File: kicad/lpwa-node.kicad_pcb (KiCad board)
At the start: 4 copper layers, 85 x 55 mm, 72 parts, among them J1 USB_C_ESP, J2 I2C, J3 USB to VBAT, J4 USB_C_SIM, J5 SIM_Card, J6 MEAS, J8 LTE, SW1 BOOT, SW2 USER, U1 TPS7A0230PDBVR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

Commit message: Draft
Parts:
- removed J2: I2C, Connector_PinHeader_2.54mm:PinHeader_2x02_P2.54mm_Vertical_SMD
- removed J3: USB to VBAT, Connector_PinHeader_2.54mm:PinHeader_1x03_P2.54mm_Vertical
- added C20: 10µF, Capacitor_SMD:C_0603_1608Metric, F.Cu at (65.0, 92.0)
- added C21: 10µF, Capacitor_SMD:C_0603_1608Metric, F.Cu at (65.8, 94.6)
- added JP11: VSYS_BYPASS, Jumper:SolderJumper-2_P1.3mm_Open_RoundedPad1.0x1.5mm, F.Cu at (53.7, 93.6)
- added R18: 100k, Resistor_SMD:R_0603_1608Metric, F.Cu at (61.5, 92.0)
- added R19: 732k, Resistor_SMD:R_0603_1608Metric, F.Cu at (61.5, 90.2)
- added R20: 1M, Resistor_SMD:R_0603_1608Metric, F.Cu at (57.5, 94.5)
- added R21: 10k, Resistor_SMD:R_0603_1608Metric, F.Cu at (57.5, 96.5)
- added TP10: SDA, TestPoint:TestPoint_Pad_D1.5mm, F.Cu at (76.5, 95.1)
- added TP11: USB_5V, TestPoint:TestPoint_Pad_D1.5mm, F.Cu at (60.5, 95.8)
- added TP12: VSYS, TestPoint:TestPoint_Pad_D1.5mm, F.Cu at (53.2, 88.0)
- added TP7: 3V0, TestPoint:TestPoint_Pad_D1.5mm, F.Cu at (53.2, 83.3)
- added TP8: GND, TestPoint:TestPoint_Pad_D1.5mm, F.Cu at (53.2, 71.0)
- added TP9: SCL, TestPoint:TestPoint_Pad_D1.5mm, F.Cu at (76.5, 93.2)
- added U10: LM66100DCK, Package_TO_SOT_SMD:SOT-363_SC-70-6, F.Cu at (57.5, 99.0)
- added U11: LM66100DCK, Package_TO_SOT_SMD:SOT-363_SC-70-6, F.Cu at (57.5, 92.0)
- added U9: TLV75901PDRVR, lpwa-node:WSON-6_L2.0-W2.0-P0.65-TL-EP, F.Cu at (63.2, 94.5)
- JP10: value SIM USB VBUS -> SIM_USB_VBUS
- moved C7 12.7 mm to (63.8, 87.0)
- moved R8 12.7 mm to (59.8, 87.0)
- moved R9 12.7 mm to (61.8, 87.0)
- moved C4 11.0 mm to (73.0, 94.5)
- moved U2 5.00 mm to (70.1, 93.6)
- moved D3 4.56 mm to (54.8, 99.0), turned to -90 degrees
- moved SW1 4.00 mm to (70.0, 87.5)
- moved C1 3.04 mm to (56.0, 89.0)
- moved U1 2.80 mm to (56.0, 85.8)
- moved C3 2.55 mm to (56.0, 82.5)
- moved TP6 1.88 mm to (76.3, 87.2)
- moved TP3 0.93 mm to (81.5, 73.4)
- moved TP5 0.70 mm to (78.3, 85.5)
- moved C2 0.50 mm to (56.0, 78.5)
- moved R2 0.50 mm to (56.0, 80.5)
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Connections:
- net +3V3 renamed 3V0
- C1 pad 2: +BATT -> VSYS
- C10 pad 2: +BATT -> VSYS
- C11 pad 2: +BATT -> VSYS
- C13 pad 2: +BATT -> VSYS
- C8 pad 2: +BATT -> VSYS
- D3 pad 1: +BATT -> BATTERY
- R8 pad 1: +BATT -> BATTERY
- U1 pad 1: +BATT -> VSYS
- U1 pad 3: +BATT -> VSYS
- U5 pad 4: +BATT -> BATTERY
- U6 pad 34: +BATT -> VSYS
- U6 pad 35: +BATT -> VSYS
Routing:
- net VSYS: track 0.00 -> 106.0 mm, vias 0 -> 6
- net +BATT: track 97.4 -> 0.00 mm, vias 5 -> 0
- net 3V0: track 160.2 -> 126.7 mm, vias 3 -> 4
- net BATTERY: track 0.00 -> 32.3 mm, vias 0 -> 3
- net /SIM7080/SIM_USB_VBUS: track 15.8 -> 30.6 mm
- net USB_ESP_+5V: track 34.9 -> 20.8 mm
- net ESP_VBAT_ADC: track 41.7 -> 30.5 mm
- net USB_4V6: track 0.00 -> 11.1 mm
- net Net-(U10-~{CE}): track 0.00 -> 10.9 mm
- net /BOOT: track 40.0 -> 45.2 mm
- net ESP_USB_D+: track 27.7 -> 22.7 mm
- net ESP_USB_D-: track 27.7 -> 22.9 mm
- net Net-(U9-FB): track 0.00 -> 4.29 mm
- net /D+: track 7.03 -> 11.3 mm
- net /D-: track 5.84 -> 8.87 mm
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- added copper zone on F.Cu, net USB_ESP_+5V
- added copper zone on F.Cu, net VSYS
- removed copper zone on F.Cu, net +BATT
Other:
- outline, holes or cut-outs redrawn
- board text added: "NiMH Rechargeable = Best Alkaline = OK Lithium 1.5V = NOT ALLOWED!"

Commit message: Draft
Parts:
- removed TP3: ESP_SIM_RI, TestPoint:TestPoint_Pad_D1.5mm
- added C22: 100µF, Capacitor_SMD:C_1206_3216Metric, F.Cu at (100.5, 46.5)
- added R23: 1M, Resistor_SMD:R_0603_1608Metric, F.Cu at (79.0, 79.5)
- added R24: 732k, Resistor_SMD:R_0603_1608Metric, F.Cu at (77.0, 79.5)
- added TP13: PWRKEY, TestPoint:TestPoint_Pad_D1.5mm, F.Cu at (93.8, 50.4)
- added TP14: STATUS, TestPoint:TestPoint_Pad_D1.5mm, F.Cu at (97.8, 52.2)
- added TP15: NETLIGHT, TestPoint:TestPoint_Pad_D1.5mm, F.Cu at (92.1, 48.5)
- moved D2 24.3 mm to (87.7, 59.8), turned to 0 degrees
- moved D4 20.4 mm to (96.0, 49.6)
- moved R1 20.2 mm to (83.0, 59.8)
- moved U4 20.0 mm to (129.0, 80.0)
- moved C6 20.0 mm to (126.0, 80.0)
- moved C1 20.0 mm to (56.0, 69.0)
- moved C10 20.0 mm to (110.0, 47.0)
- moved C11 20.0 mm to (106.5, 46.5)
- moved C12 20.0 mm to (89.2, 51.5)
- moved C13 20.0 mm to (103.5, 46.5)
- moved C14 20.0 mm to (82.5, 78.6)
- moved C15 20.0 mm to (102.0, 74.5)
- moved C17 20.0 mm to (123.0, 55.0)
- moved C19 20.0 mm to (125.5, 52.5)
- moved C2 20.0 mm to (56.0, 58.5)
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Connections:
- U3 pad 18: ESP_SIM_RI -> ESP_USB_SENSE
- U6 pad 41: unconnected-(U6-NETLIGHT-Pad41) -> Net-(U6-NETLIGHT)
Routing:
- net ESP_USB_SENSE: track 0.00 -> 40.3 mm, vias 0 -> 2
- net VSYS: track 106.0 -> 83.1 mm, vias 6 -> 7
- net Net-(U6-NETLIGHT): track 0.00 -> 15.5 mm, vias 0 -> 2
- net USB_ESP_+5V: track 20.8 -> 33.2 mm
- net 3V0: track 126.7 -> 117.8 mm
- net GND: track 21.2 -> 16.1 mm, vias 90 -> 105
- net SCL: track 94.1 -> 89.7 mm
- net ESP_SIM_RI: track 4.07 -> 0.00 mm
- net SIM_STATUS: track 7.88 -> 11.0 mm
- net Net-(U5-Pad2): track 77.8 -> 79.2 mm
- net ESP_BTN: track 22.5 -> 23.5 mm
- net SIM_PWRKEY: track 44.6 -> 45.4 mm
- net SDA: track 80.3 -> 81.0 mm
- added copper zone on F.Cu, net 3V0
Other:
- board size 85 x 55 mm -> 84 x 50 mm
- board text added: "ENGINEERING SAMPLE NOT FOR RESALE NOT CERTIFIED"
- board text added: "https://github.com/MikkoTervala/ lpwa-node-hardware"
- board text added: "⌀ 2.6mm"
- board text removed: "NiMH Rechargeable = Best Alkaline = OK Lithium 1.5V = NOT ALLOWED!"

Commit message: First orderable version
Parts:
- added D7: ESD5Z3.3T1G, Diode_SMD:D_SOD-523, F.Cu at (115.5, 80.0)
- added D8: ESD5Z3.3T1G, Diode_SMD:D_SOD-523, F.Cu at (112.0, 80.0)
- added D9: ESD5Z3.3T1G, Diode_SMD:D_SOD-523, F.Cu at (113.8, 80.0)
- added R22: 10k, Resistor_SMD:R_0603_1608Metric, F.Cu at (89.2, 49.5)
- added R25: 100k, Resistor_SMD:R_0603_1608Metric, F.Cu at (90.0, 59.2)
- C6: value 100nF -> 10µF
- moved R14 4.60 mm to (112.8, 74.8), turned to 180 degrees
- moved R13 2.26 mm to (112.8, 76.8), turned to 0 degrees
- moved R6 1.53 mm to (93.9, 58.4)
- moved R7 1.53 mm to (93.9, 56.9)
- moved TP1 1.22 mm to (96.7, 57.0)
- moved TP2 1.22 mm to (96.7, 54.5)
- moved TP4 1.22 mm to (96.7, 59.5)
- moved D2 1.08 mm to (86.8, 59.2)
- moved JP10 1.00 mm to (109.0, 73.1)
- moved R11 1.00 mm to (97.6, 70.3)
- moved R1 0.60 mm to (83.0, 59.2)
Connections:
- D4 pad 1: SIM_PWRKEY -> Net-(D4-K)
- TP13 pad 1: SIM_PWRKEY -> Net-(D4-K)
- U6 pad 39: SIM_PWRKEY -> Net-(D4-K)
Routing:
- net SIM_PWRKEY: track 45.4 -> 26.5 mm
- net Net-(D4-K): track 0.00 -> 18.0 mm
- net 3V0: track 117.8 -> 125.1 mm
- net ESP_BTN: track 23.5 -> 27.0 mm
- net SDA: track 81.0 -> 83.5 mm, vias 2 -> 4
- net Net-(J4-CC2): track 9.77 -> 7.25 mm
- net /BOOT: track 45.2 -> 46.8 mm
- net SCL: track 89.7 -> 91.1 mm, vias 3 -> 5
- net Net-(J4-CC1): track 11.6 -> 10.3 mm
- net Net-(D1-A): track 7.21 -> 8.25 mm
- net USB_SIM_+5V: track 13.6 -> 14.1 mm
- net /SIM7080/SIM_USB_VBUS: track 30.6 -> 30.1 mm
- net GND: vias 105 -> 108

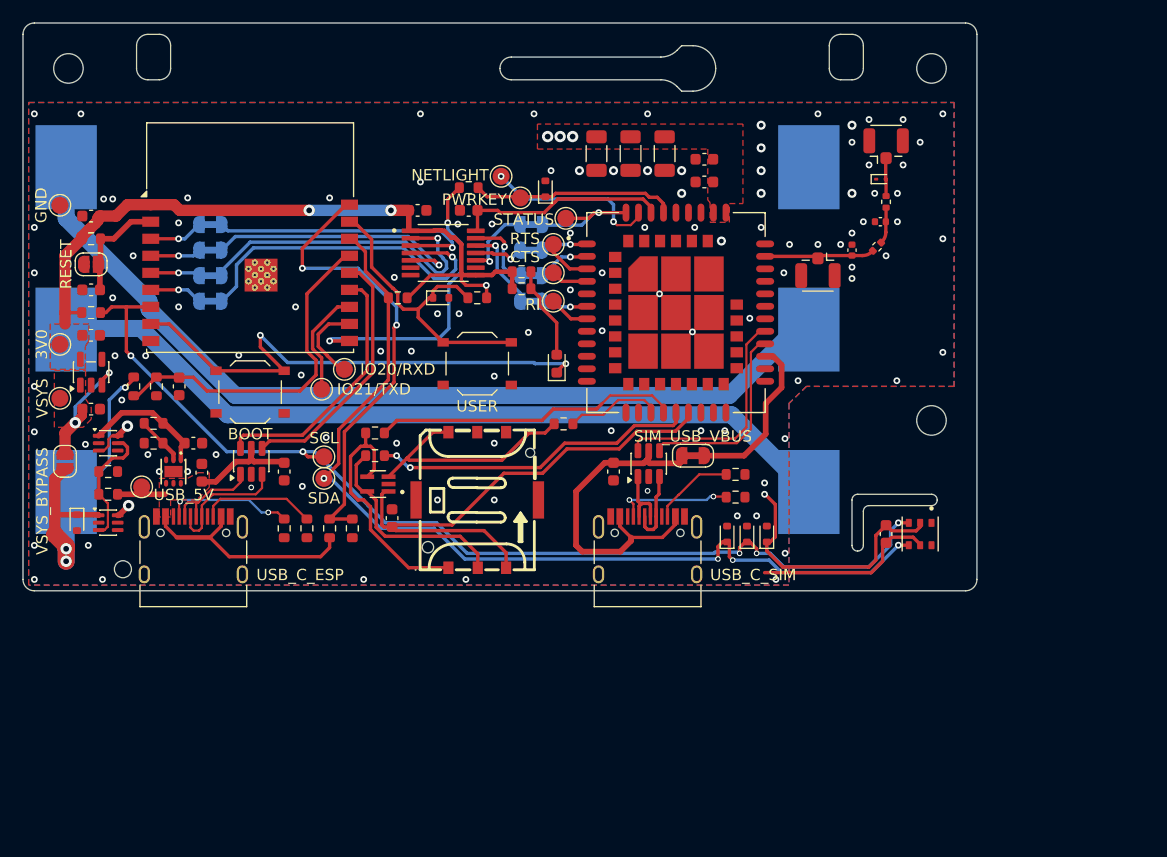
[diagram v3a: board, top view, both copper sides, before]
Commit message: Optimize for manufacturing, add part numbers
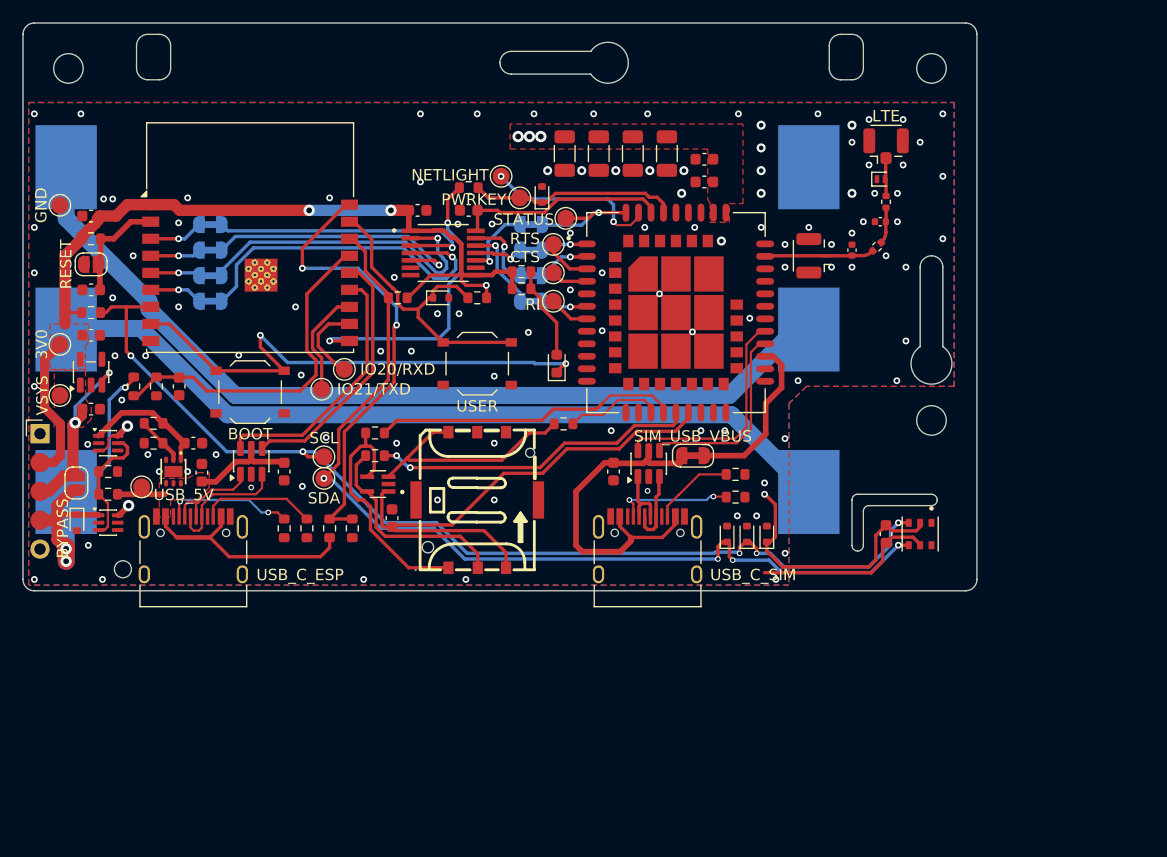
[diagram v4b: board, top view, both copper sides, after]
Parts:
- added C23: 100µF, Capacitor_SMD:C_1206_3216Metric, F.Cu at (97.7, 46.5)
- added J2: Manufacturing Jig, lpwa-node:TestHeader_1x05_P2.54mm, F.Cu at (51.5, 71.2)
- D6: footprint Diode_SMD:D_SOD-923 -> Diode_SMD:D_SOD-882
- J6: footprint Connector_Coaxial:U.FL_Hirose_U.FL-R-SMT-1_Vertical -> lpwa-node:U.FL_Hirose_MEAS
- JP11: value VSYS_BYPASS -> BYPASS
- moved JP11 2.15 mm to (54.7, 75.5)
- moved J6 1.92 mm to (119.2, 55.5), turned to 180 degrees
- moved D4 0.58 mm to (95.7, 50.1)
- moved TP12 0.25 mm to (53.2, 67.8)
- moved C11 0.20 mm to (106.7, 46.5)
- moved C13 0.20 mm to (103.7, 46.5)
- moved C22 0.20 mm to (100.7, 46.5)
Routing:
- net 3V0: track 125.1 -> 138.1 mm
- net VSYS: track 83.1 -> 85.0 mm
- net GND: vias 108 -> 111
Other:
- outline, holes or cut-outs redrawn

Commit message: Release A
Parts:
- added T1: Tab, PCM_kikit:Tab, F.Cu at (55.0, 35.0)
- added T2: Tab, PCM_kikit:Tab, F.Cu at (55.0, 85.0)
- added T3: Tab, PCM_kikit:Tab, F.Cu at (114.0, 35.0)
- added T4: Tab, PCM_kikit:Tab, F.Cu at (114.0, 85.0)
- moved D6 0.10 mm to (125.6, 48.8)
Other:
- board text added: "Release A 06/2026"
